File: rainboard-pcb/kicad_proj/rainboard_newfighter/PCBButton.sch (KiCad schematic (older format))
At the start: 4 parts, among them SW17 SANWA-OBSF24

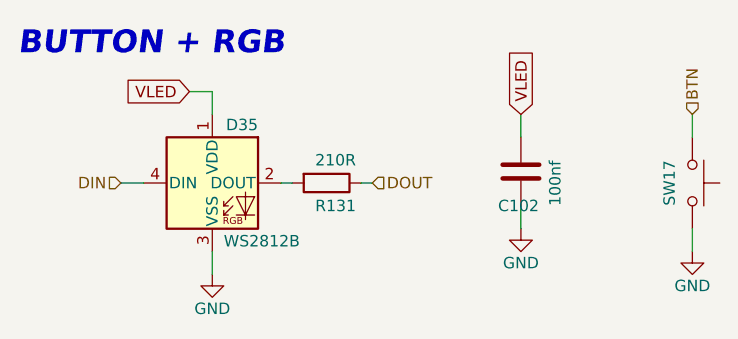
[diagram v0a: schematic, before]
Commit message: Minor schematic and library changes
Identical to previous commit, some files weren't saved.
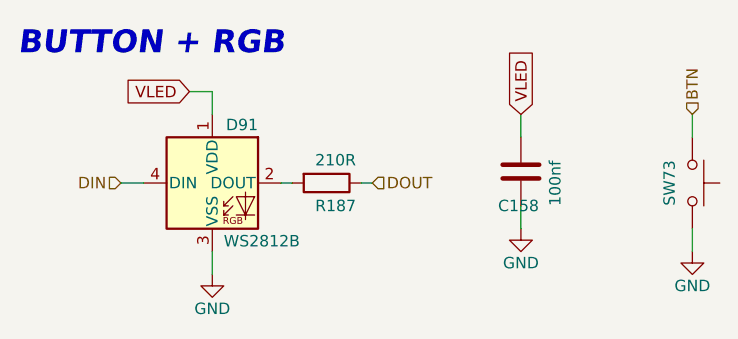
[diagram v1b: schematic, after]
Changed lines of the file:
@@
 AR Path="/6016C70A/6001C20F/5FE1B43A" Ref="SW?"  Part="1"
 AR Path="/6016C70A/6001C223/5FE1B43A" Ref="SW?"  Part="1"
-F 0 "SW17" H 3600 1300 50  0000 C CNN
+F 0 "SW73" H 3600 1300 50  0000 C CNN
 F 1 "SANWA-OBSF24" H 3600 1340 50  0001 C CNN
 F 2 "" H 3600 1600 50  0001 C CNN
@@
 AR Path="/6016C70A/6001C20F/5FE1B440" Ref="D?"  Part="1"
 AR Path="/6016C70A/6001C223/5FE1B440" Ref="D?"  Part="1"
-F 0 "D35" H 1700 1625 50  0000 R BNN
+F 0 "D91" H 1700 1625 50  0000 R BNN
 F 1 "WS2812B" H 1550 1175 50  0000 L TNN
 F 2 "LED_SMD:LED_WS2812B_PLCC4_5.0x5.0mm_P3.2mm" H 1550 1100 50  0001 L TNN
@@
 AR Path="/6016C70A/6001C20F/5FE1B462" Ref="R?"  Part="1"
 AR Path="/6016C70A/6001C223/5FE1B462" Ref="R?"  Part="1"
-F 0 "R131" V 2100 1350 50  0000 L CNN
+F 0 "R187" V 2100 1350 50  0000 L CNN
 F 1 "210R" V 1900 1350 50  0000 L CNN
 F 2 "Resistor_SMD:R_0805_2012Metric" V 1930 1400 50  0001 C CNN
@@
 AR Path="/6016C70A/6001C20F/5FE25316" Ref="C?"  Part="1"
 AR Path="/6016C70A/6001C223/5FE25316" Ref="C?"  Part="1"
-F 0 "C102" H 2750 1200 50  0000 L CNN
+F 0 "C158" H 2750 1200 50  0000 L CNN
 F 1 "100nf" V 3000 1200 50  0000 L CNN
 F 2 "Capacitor_SMD:C_0603_1608Metric" H 2888 1200 50  0001 C CNN

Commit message: Removed RGB from buttons, part numbers updated, cleaned up schematic
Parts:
- C102: PN (none) -> CC0603KRX7R9BB104
- D35: PN (none) -> WS2812B
- R131: PN (none) -> RC0603FR-07210RL
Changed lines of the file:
@@
 $Descr A4 11693 8268
 encoding utf-8
-Sheet 8 65
+Sheet 8 59
 Title ""
 Date ""
@@
 F 2 "LED_SMD:LED_WS2812B_PLCC4_5.0x5.0mm_P3.2mm" H 1550 1100 50  0001 L TNN
 F 3 "https://cdn-shop.adafruit.com/datasheets/WS2812B.pdf" H 1600 1025 50  0001 L TNN
+F 4 "WS2812B" H 1500 1400 50  0001 C CNN "PN"
 	1    1500 1400
 	1    0    0    -1
@@
 F 3 "~" H 2000 1400 50  0001 C CNN
 F 4 "C228630" H 2000 1400 50  0001 C CNN "LCSC"
+F 5 "RC0603FR-07210RL" H 2000 1400 50  0001 C CNN "PN"
 	1    2000 1400
 	0    1    1    0
@@
 F 3 "~" H 2850 1350 50  0001 C CNN
 F 4 "C14663" H 2850 1350 50  0001 C CNN "LCSC"
+F 5 "CC0603KRX7R9BB104" H 2850 1350 50  0001 C CNN "PN"
 	1    2850 1350
 	1    0    0    -1

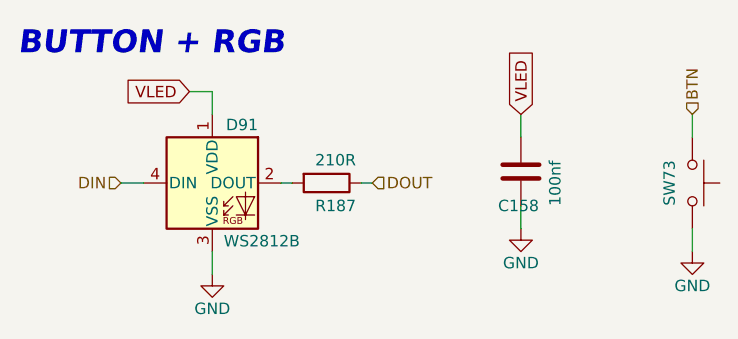
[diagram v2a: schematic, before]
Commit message: New footprints added
Updated library format for footprints. Pending sync with layout to add all new footprints
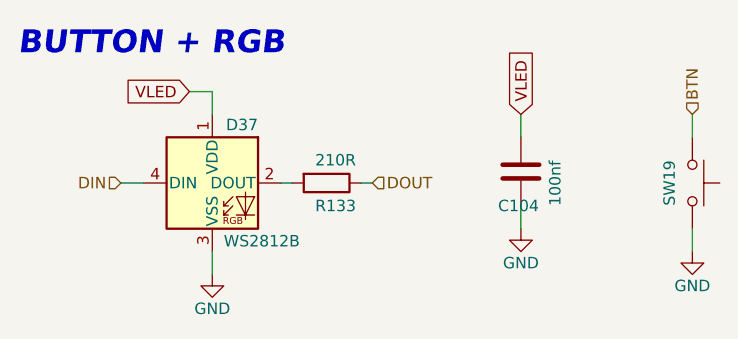
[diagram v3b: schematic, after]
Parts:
- SW17: footprint (none) -> rainboard_fp:Sanwa-OBSF24-v2
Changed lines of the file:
@@
 AR Path="/6016C70A/6001C20F/5FE1B43A" Ref="SW?"  Part="1"
 AR Path="/6016C70A/6001C223/5FE1B43A" Ref="SW?"  Part="1"
-F 0 "SW73" H 3600 1300 50  0000 C CNN
+F 0 "SW19" H 3600 1300 50  0000 C CNN
 F 1 "SANWA-OBSF24" H 3600 1340 50  0001 C CNN
-F 2 "" H 3600 1600 50  0001 C CNN
+F 2 "rainboard_fp:Sanwa-OBSF24-v2" H 3600 1600 50  0001 C CNN
 F 3 "" H 3600 1600 50  0001 C CNN
 F 4 "SANWA-OBSC-CW/W" H 3600 1400 50  0001 C CNN "PN"
@@
 AR Path="/6016C70A/6001C20F/5FE1B440" Ref="D?"  Part="1"
 AR Path="/6016C70A/6001C223/5FE1B440" Ref="D?"  Part="1"
-F 0 "D91" H 1700 1625 50  0000 R BNN
+F 0 "D37" H 1700 1625 50  0000 R BNN
 F 1 "WS2812B" H 1550 1175 50  0000 L TNN
 F 2 "LED_SMD:LED_WS2812B_PLCC4_5.0x5.0mm_P3.2mm" H 1550 1100 50  0001 L TNN
@@
 AR Path="/6016C70A/6001C20F/5FE1B462" Ref="R?"  Part="1"
 AR Path="/6016C70A/6001C223/5FE1B462" Ref="R?"  Part="1"
-F 0 "R187" V 2100 1350 50  0000 L CNN
+F 0 "R133" V 2100 1350 50  0000 L CNN
 F 1 "210R" V 1900 1350 50  0000 L CNN
 F 2 "Resistor_SMD:R_0805_2012Metric" V 1930 1400 50  0001 C CNN
@@
 AR Path="/6016C70A/6001C20F/5FE25316" Ref="C?"  Part="1"
 AR Path="/6016C70A/6001C223/5FE25316" Ref="C?"  Part="1"
-F 0 "C158" H 2750 1200 50  0000 L CNN
+F 0 "C104" H 2750 1200 50  0000 L CNN
 F 1 "100nf" V 3000 1200 50  0000 L CNN
 F 2 "Capacitor_SMD:C_0603_1608Metric" H 2888 1200 50  0001 C CNN

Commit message: Fixing annotations for buttons and meta buttons
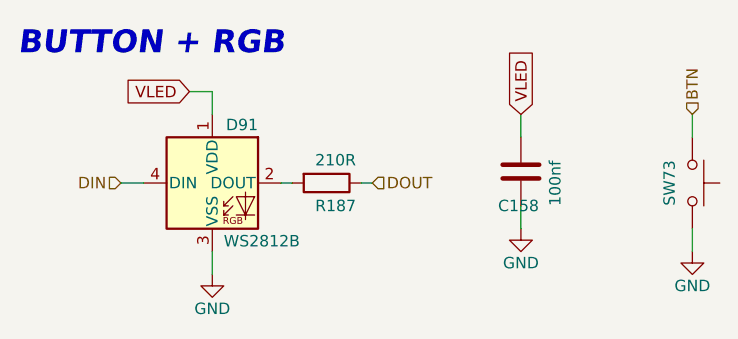
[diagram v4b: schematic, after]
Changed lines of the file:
@@
 $Descr A4 11693 8268
 encoding utf-8
-Sheet 8 59
+Sheet 59 59
 Title ""
 Date ""
@@
 AR Path="/6016C70A/6001C20F/5FE1B43A" Ref="SW?"  Part="1"
 AR Path="/6016C70A/6001C223/5FE1B43A" Ref="SW?"  Part="1"
-F 0 "SW19" H 3600 1300 50  0000 C CNN
+F 0 "SW73" H 3600 1300 50  0000 C CNN
 F 1 "SANWA-OBSF24" H 3600 1340 50  0001 C CNN
 F 2 "rainboard_fp:Sanwa-OBSF24-v2" H 3600 1600 50  0001 C CNN
@@
 AR Path="/6016C70A/6001C20F/5FE1B440" Ref="D?"  Part="1"
 AR Path="/6016C70A/6001C223/5FE1B440" Ref="D?"  Part="1"
-F 0 "D37" H 1700 1625 50  0000 R BNN
+F 0 "D91" H 1700 1625 50  0000 R BNN
 F 1 "WS2812B" H 1550 1175 50  0000 L TNN
 F 2 "LED_SMD:LED_WS2812B_PLCC4_5.0x5.0mm_P3.2mm" H 1550 1100 50  0001 L TNN
@@
 AR Path="/6016C70A/6001C20F/5FE1B462" Ref="R?"  Part="1"
 AR Path="/6016C70A/6001C223/5FE1B462" Ref="R?"  Part="1"
-F 0 "R133" V 2100 1350 50  0000 L CNN
+F 0 "R187" V 2100 1350 50  0000 L CNN
 F 1 "210R" V 1900 1350 50  0000 L CNN
 F 2 "Resistor_SMD:R_0805_2012Metric" V 1930 1400 50  0001 C CNN
@@
 AR Path="/6016C70A/6001C20F/5FE25316" Ref="C?"  Part="1"
 AR Path="/6016C70A/6001C223/5FE25316" Ref="C?"  Part="1"
-F 0 "C104" H 2750 1200 50  0000 L CNN
+F 0 "C158" H 2750 1200 50  0000 L CNN
 F 1 "100nf" V 3000 1200 50  0000 L CNN
 F 2 "Capacitor_SMD:C_0603_1608Metric" H 2888 1200 50  0001 C CNN

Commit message: Moves meta buttons to correct config, adds back on board buttons.
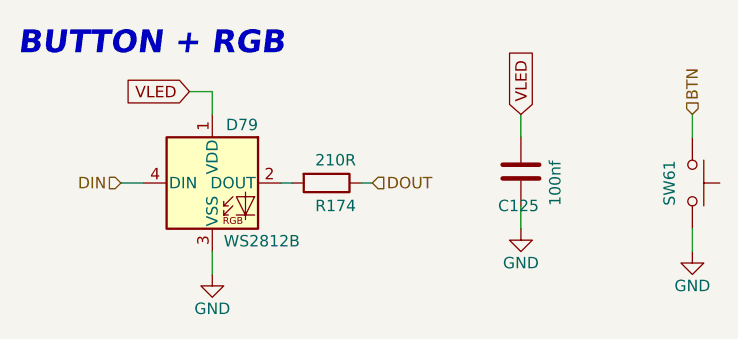
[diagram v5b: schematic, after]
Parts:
- renumbered C102 to C65, D35 to D19, R131 to R114, SW17 to SW1

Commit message: Swaps over to 5V  input supply
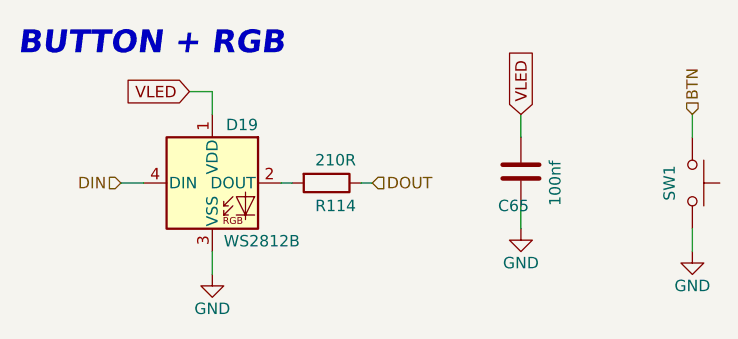
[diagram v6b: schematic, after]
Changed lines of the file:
@@
 $Descr A4 11693 8268
 encoding utf-8
-Sheet 60 63
+Sheet 3 63
 Title ""
 Date ""
@@
 AR Path="/6016C70A/611F5597/5FE1B43A" Ref="SW60"  Part="1"
 AR Path="/6016C70A/6120995F/5FE1B43A" Ref="SW61"  Part="1"
-F 0 "SW61" H 3600 1300 50  0000 C CNN
+F 0 "SW1" H 3600 1300 50  0000 C CNN
 F 1 "SANWA-OBSF24" H 3600 1340 50  0001 C CNN
 F 2 "rainboard_fp:Sanwa-OBSF24-v2" H 3600 1600 50  0001 C CNN
@@
 AR Path="/6016C70A/611F5597/5FE1B440" Ref="D78"  Part="1"
 AR Path="/6016C70A/6120995F/5FE1B440" Ref="D79"  Part="1"
-F 0 "D79" H 1700 1625 50  0000 R BNN
+F 0 "D19" H 1700 1625 50  0000 R BNN
 F 1 "WS2812B" H 1550 1175 50  0000 L TNN
 F 2 "LED_SMD:LED_WS2812B_PLCC4_5.0x5.0mm_P3.2mm" H 1550 1100 50  0001 L TNN
@@
 AR Path="/6016C70A/611F5597/5FE1B462" Ref="R173"  Part="1"
 AR Path="/6016C70A/6120995F/5FE1B462" Ref="R174"  Part="1"
-F 0 "R174" V 2100 1350 50  0000 L CNN
+F 0 "R114" V 2100 1350 50  0000 L CNN
 F 1 "210R" V 1900 1350 50  0000 L CNN
 F 2 "Resistor_SMD:R_0805_2012Metric" V 1930 1400 50  0001 C CNN
@@
 AR Path="/6016C70A/611F5597/5FE25316" Ref="C124"  Part="1"
 AR Path="/6016C70A/6120995F/5FE25316" Ref="C125"  Part="1"
-F 0 "C125" H 2750 1200 50  0000 L CNN
+F 0 "C65" H 2750 1200 50  0000 L CNN
 F 1 "100nf" V 3000 1200 50  0000 L CNN
 F 2 "Capacitor_SMD:C_0603_1608Metric" H 2888 1200 50  0001 C CNN

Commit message: Modified electrolytics and setup board for layout
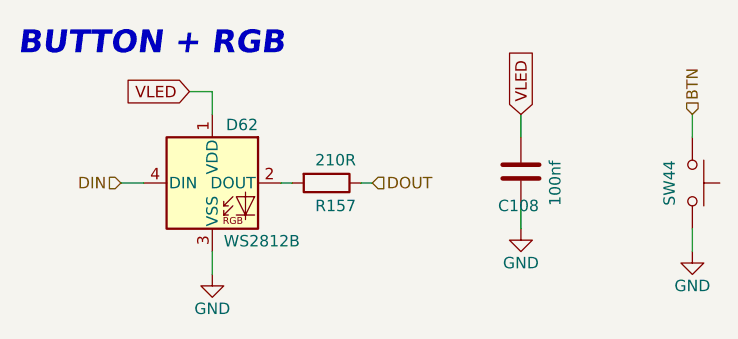
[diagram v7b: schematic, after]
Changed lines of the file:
@@
 $Descr A4 11693 8268
 encoding utf-8
-Sheet 3 63
+Sheet 46 63
 Title ""
 Date ""
@@
 AR Path="/6016C70A/611F5597/5FE1B43A" Ref="SW60"  Part="1"
 AR Path="/6016C70A/6120995F/5FE1B43A" Ref="SW61"  Part="1"
-F 0 "SW1" H 3600 1300 50  0000 C CNN
+F 0 "SW44" H 3600 1300 50  0000 C CNN
 F 1 "SANWA-OBSF24" H 3600 1340 50  0001 C CNN
 F 2 "rainboard_fp:Sanwa-OBSF24-v2" H 3600 1600 50  0001 C CNN
@@
 AR Path="/6016C70A/611F5597/5FE1B440" Ref="D78"  Part="1"
 AR Path="/6016C70A/6120995F/5FE1B440" Ref="D79"  Part="1"
-F 0 "D19" H 1700 1625 50  0000 R BNN
+F 0 "D62" H 1700 1625 50  0000 R BNN
 F 1 "WS2812B" H 1550 1175 50  0000 L TNN
 F 2 "LED_SMD:LED_WS2812B_PLCC4_5.0x5.0mm_P3.2mm" H 1550 1100 50  0001 L TNN
@@
 AR Path="/6016C70A/611F5597/5FE1B446" Ref="#PWR0291"  Part="1"
 AR Path="/6016C70A/6120995F/5FE1B446" Ref="#PWR0294"  Part="1"
-F 0 "#PWR0294" H 3600 1450 50  0001 C CNN
+F 0 "#PWR0243" H 3600 1450 50  0001 C CNN
 F 1 "GND" H 3600 1550 50  0000 C CNN
 F 2 "" H 3600 1700 50  0001 C CNN
@@
 AR Path="/6016C70A/611F5597/5FE1B44C" Ref="#PWR0289"  Part="1"
 AR Path="/6016C70A/6120995F/5FE1B44C" Ref="#PWR0292"  Part="1"
-F 0 "#PWR0292" H 1500 1550 50  0001 C CNN
+F 0 "#PWR0241" H 1500 1550 50  0001 C CNN
 F 1 "GND" H 1500 1650 50  0000 C CNN
 F 2 "" H 1500 1800 50  0001 C CNN
@@
 AR Path="/6016C70A/611F5597/5FE1B462" Ref="R173"  Part="1"
 AR Path="/6016C70A/6120995F/5FE1B462" Ref="R174"  Part="1"
-F 0 "R114" V 2100 1350 50  0000 L CNN
+F 0 "R157" V 2100 1350 50  0000 L CNN
 F 1 "210R" V 1900 1350 50  0000 L CNN
 F 2 "Resistor_SMD:R_0805_2012Metric" V 1930 1400 50  0001 C CNN
@@
 AR Path="/6016C70A/611F5597/5FE25316" Ref="C124"  Part="1"
 AR Path="/6016C70A/6120995F/5FE25316" Ref="C125"  Part="1"
-F 0 "C65" H 2750 1200 50  0000 L CNN
+F 0 "C108" H 2750 1200 50  0000 L CNN
 F 1 "100nf" V 3000 1200 50  0000 L CNN
 F 2 "Capacitor_SMD:C_0603_1608Metric" H 2888 1200 50  0001 C CNN
@@
 AR Path="/6016C70A/611F5597/5FE292FC" Ref="#PWR0290"  Part="1"
 AR Path="/6016C70A/6120995F/5FE292FC" Ref="#PWR0293"  Part="1"
-F 0 "#PWR0293" H 2850 1350 50  0001 C CNN
+F 0 "#PWR0242" H 2850 1350 50  0001 C CNN
 F 1 "GND" H 2850 1450 50  0000 C CNN
 F 2 "" H 2850 1600 50  0001 C CNN

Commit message: prelim place & route
deleted extra R's layout & sch
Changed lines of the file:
@@
 $Descr A4 11693 8268
 encoding utf-8
-Sheet 46 63
+Sheet 21 63
 Title ""
 Date ""
@@
 AR Path="/6016C70A/611F5597/5FE1B43A" Ref="SW60"  Part="1"
 AR Path="/6016C70A/6120995F/5FE1B43A" Ref="SW61"  Part="1"
-F 0 "SW44" H 3600 1300 50  0000 C CNN
+F 0 "SW19" H 3600 1300 50  0000 C CNN
 F 1 "SANWA-OBSF24" H 3600 1340 50  0001 C CNN
 F 2 "rainboard_fp:Sanwa-OBSF24-v2" H 3600 1600 50  0001 C CNN
@@
 AR Path="/6016C70A/611F5597/5FE1B440" Ref="D78"  Part="1"
 AR Path="/6016C70A/6120995F/5FE1B440" Ref="D79"  Part="1"
-F 0 "D62" H 1700 1625 50  0000 R BNN
+F 0 "D37" H 1700 1625 50  0000 R BNN
 F 1 "WS2812B" H 1550 1175 50  0000 L TNN
 F 2 "LED_SMD:LED_WS2812B_PLCC4_5.0x5.0mm_P3.2mm" H 1550 1100 50  0001 L TNN
@@
 AR Path="/6016C70A/611F5597/5FE1B446" Ref="#PWR0291"  Part="1"
 AR Path="/6016C70A/6120995F/5FE1B446" Ref="#PWR0294"  Part="1"
-F 0 "#PWR0243" H 3600 1450 50  0001 C CNN
+F 0 "#PWR0168" H 3600 1450 50  0001 C CNN
 F 1 "GND" H 3600 1550 50  0000 C CNN
 F 2 "" H 3600 1700 50  0001 C CNN
@@
 AR Path="/6016C70A/611F5597/5FE1B44C" Ref="#PWR0289"  Part="1"
 AR Path="/6016C70A/6120995F/5FE1B44C" Ref="#PWR0292"  Part="1"
-F 0 "#PWR0241" H 1500 1550 50  0001 C CNN
+F 0 "#PWR0166" H 1500 1550 50  0001 C CNN
 F 1 "GND" H 1500 1650 50  0000 C CNN
 F 2 "" H 1500 1800 50  0001 C CNN
@@
 AR Path="/6016C70A/611F5597/5FE1B462" Ref="R173"  Part="1"
 AR Path="/6016C70A/6120995F/5FE1B462" Ref="R174"  Part="1"
-F 0 "R157" V 2100 1350 50  0000 L CNN
+F 0 "R132" V 2100 1350 50  0000 L CNN
 F 1 "210R" V 1900 1350 50  0000 L CNN
 F 2 "Resistor_SMD:R_0805_2012Metric" V 1930 1400 50  0001 C CNN
@@
 AR Path="/6016C70A/611F5597/5FE25316" Ref="C124"  Part="1"
 AR Path="/6016C70A/6120995F/5FE25316" Ref="C125"  Part="1"
-F 0 "C108" H 2750 1200 50  0000 L CNN
+F 0 "C83" H 2750 1200 50  0000 L CNN
 F 1 "100nf" V 3000 1200 50  0000 L CNN
 F 2 "Capacitor_SMD:C_0603_1608Metric" H 2888 1200 50  0001 C CNN
@@
 AR Path="/6016C70A/611F5597/5FE292FC" Ref="#PWR0290"  Part="1"
 AR Path="/6016C70A/6120995F/5FE292FC" Ref="#PWR0293"  Part="1"
-F 0 "#PWR0242" H 2850 1350 50  0001 C CNN
+F 0 "#PWR0167" H 2850 1350 50  0001 C CNN
 F 1 "GND" H 2850 1450 50  0000 C CNN
 F 2 "" H 2850 1600 50  0001 C CNN
